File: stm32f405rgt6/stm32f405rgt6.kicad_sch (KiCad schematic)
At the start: 41 parts, among them J1 USART, J2 SWD, J3 I2C, J4 USB_OTG, J5 SPI, J6 AnalogInptus, J7 5V, J8 CAN, J9 3.3V, SW1 SW_Push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

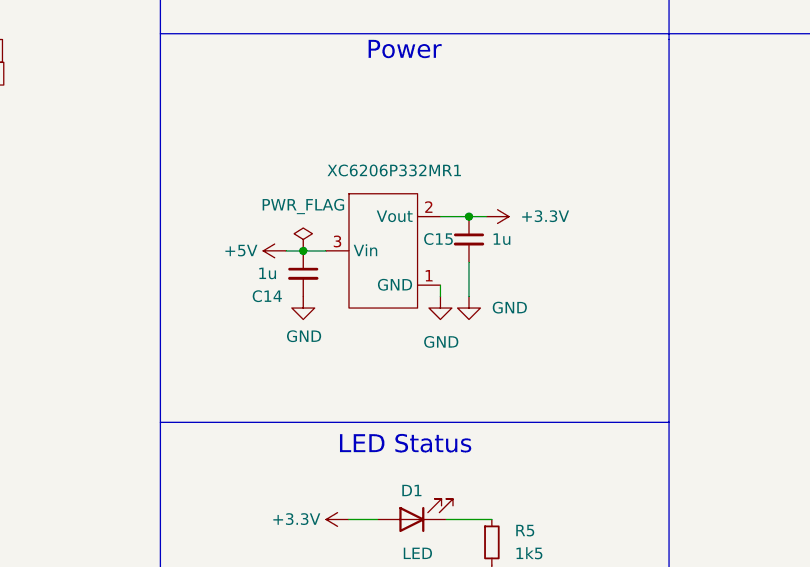
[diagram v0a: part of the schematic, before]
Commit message: reverted back to a version where the caps were not added to the voltage regulator
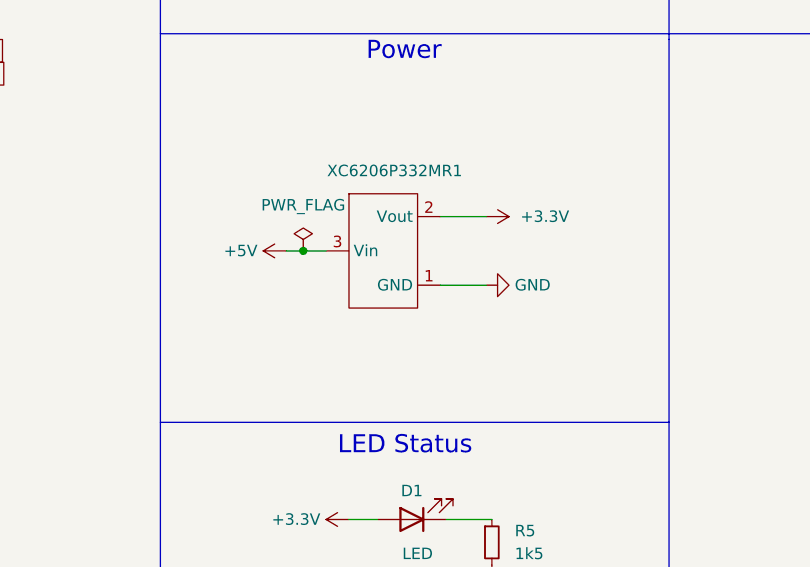
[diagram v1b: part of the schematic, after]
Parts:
- removed C14, C15: 1u, Capacitor_SMD:C_0603_1608Metric, symbol Device:C_Small
- J1: footprint Connector_PinHeader_2.54mm:PinHeader_1x04_P2.54mm_Vertical -> Connector_PinHeader_1.27mm:PinHeader_1x04_P1.27mm_Vertical
- J5: footprint TerminalBlock_Phoenix:TerminalBlock_Phoenix_MKDS-1,5-6_1x06_P5.00mm_Horizontal -> TerminalBlock_Phoenix:TerminalBlock_Phoenix_MKDS-1,5-6-5.08_1x06_P5.08mm_Horizontal
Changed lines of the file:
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@@
   (junction (at 20.955 72.39) (diameter 0) (color 0 0 0 0)
-  )
-  (junction (at 183.515 120.65) (diameter 0) (color 0 0 0 0)
   )
   (junction (at 41.91 167.64) (diameter 0) (color 0 0 0 0)
@@
     (stroke (width 0) (type default))
   )
+  (wire (pts (xy 180.34 128.27) (xy 185.42 128.27))
+    (stroke (width 0) (type default))
+  )
   (polyline (pts (xy 205.74 143.51) (xy 149.225 143.51))
     (stroke (width 0) (type default))
@@
     (stroke (width 0) (type default))
   )
-  (wire (pts (xy 183.515 129.54) (xy 183.515 125.73))
-    (stroke (width 0) (type default))
-  )
   (wire (pts (xy 22.86 146.685) (xy 45.085 146.685))
     (stroke (width 0) (type default))
@@
     (stroke (width 0) (type default))
   )
-  (wire (pts (xy 183.515 120.65) (xy 185.42 120.65))
-    (stroke (width 0) (type default))
-  )
   (wire (pts (xy 188.595 37.465) (xy 188.595 39.37))
     (stroke (width 0) (type default))
@@
     (stroke (width 0) (type default))
   )
-  (wire (pts (xy 180.34 129.54) (xy 180.34 128.27))
-    (stroke (width 0) (type default))
-  )
   (wire (pts (xy 99.06 90.17) (xy 101.6 90.17))
     (stroke (width 0) (type default))
@@
     (stroke (width 0) (type default))
   )
-  (wire (pts (xy 180.34 120.65) (xy 183.515 120.65))
+  (wire (pts (xy 180.34 120.65) (xy 185.42 120.65))
     (stroke (width 0) (type default))
   )
@@
     )
   )
-  (symbol (lib_id "power:GND") (at 165.1 129.54 0) (unit 1)
-    (in_bom yes) (on_board yes) (dnp no)
-    (property "Reference" "#PWR045" (at 165.1 135.89 0)
-      (effects (font (size 1.27 1.27)) hide)
-    )
-    (property "Value" "GND" (at 163.195 133.985 0)
-      (effects (font (size 1.27 1.27)) (justify left))
-    )
-    (property "Footprint" "" (at 165.1 129.54 0)
-      (effects (font (size 1.27 1.27)) hide)
-    )
-    (property "Datasheet" "" (at 165.1 129.54 0)
-      (effects (font (size 1.27 1.27)) hide)
-    )
-    (pin "1")
-    (instances
-      (project "stm32f405rgt6"
-        (path "/521c39b3-5842-46c1-bbd0-ab8aad1ee68c"
-          (reference "#PWR045") (unit 1)
-        )
-      )
-    )
-  )
   (symbol (lib_id "Custom:XC6206P332MR") (at 173.99 124.46 0) (unit 1)
     (in_bom yes) (on_board yes) (dnp no) (fields_autoplaced)
@@
       (effects (font (size 1.27 1.27)))
     )
-    (property "Footprint" "Connector_PinHeader_2.54mm:PinHeader_1x04_P2.54mm_Vertical" (at 24.765 37.465 0)
+    (property "Footprint" "Connector_PinHeader_1.27mm:PinHeader_1x04_P1.27mm_Vertical" (at 24.765 37.465 0)
       (effects (font (size 1.27 1.27)) hide)
     )
@@
     )
   )
-  (symbol (lib_id "power:GND") (at 180.34 129.54 0) (unit 1)
-    (in_bom yes) (on_board yes) (dnp no)
-    (property "Reference" "#PWR025" (at 180.34 135.89 0)
-      (effects (font (size 1.27 1.27)) hide)
-    )
-    (property "Value" "GND" (at 178.435 134.62 0)
-      (effects (font (size 1.27 1.27)) (justify left))
-    )
-    (property "Footprint" "" (at 180.34 129.54 0)
-      (effects (font (size 1.27 1.27)) hide)
-    )
-    (property "Datasheet" "" (at 180.34 129.54 0)
+  (symbol (lib_id "power:GND") (at 185.42 128.27 90) (unit 1)
+    (in_bom yes) (on_board yes) (dnp no) (fields_autoplaced)
+    (property "Reference" "#PWR025" (at 191.77 128.27 0)
+      (effects (font (size 1.27 1.27)) hide)
+    )
+    (property "Value" "GND" (at 188.595 128.27 90)
+      (effects (font (size 1.27 1.27)) (justify right))
+    )
+    (property "Footprint" "" (at 185.42 128.27 0)
+      (effects (font (size 1.27 1.27)) hide)
+    )
+    (property "Datasheet" "" (at 185.42 128.27 0)
       (effects (font (size 1.27 1.27)) hide)
     )
@@
         (path "/521c39b3-5842-46c1-bbd0-ab8aad1ee68c"
           (reference "C4") (unit 1)
-        )
-      )
-    )
-  )
-  (symbol (lib_id "Device:C_Small") (at 183.515 123.19 0) (unit 1)
-    (in_bom yes) (on_board yes) (dnp no)
-    (property "Reference" "C15" (at 178.435 123.19 0)
-      (effects (font (size 1.27 1.27)) (justify left))
-    )
-    (property "Value" "1u" (at 186.055 123.19 0)
-      (effects (font (size 1.27 1.27)) (justify left))
-    )
-    (property "Footprint" "Capacitor_SMD:C_0603_1608Metric" (at 183.515 123.19 0)
-      (effects (font (size 1.27 1.27)) hide)
-    )
-    (property "Datasheet" "~" (at 183.515 123.19 0)
-      (effects (font (size 1.27 1.27)) hide)
-    )
-    (pin "1")
-    (pin "2")
-    (instances
-      (project "stm32f405rgt6"
-        (path "/521c39b3-5842-46c1-bbd0-ab8aad1ee68c"
-          (reference "C15") (unit 1)
         )
       )
@@
     )
   )
-  (symbol (lib_id "Device:C_Small") (at 165.1 127 0) (unit 1)
-    (in_bom yes) (on_board yes) (dnp no)
-    (property "Reference" "C14" (at 159.385 129.54 0)
-      (effects (font (size 1.27 1.27)) (justify left))
-    )
-    (property "Value" "1u" (at 160.02 127 0)
-      (effects (font (size 1.27 1.27)) (justify left))
-    )
-    (property "Footprint" "Capacitor_SMD:C_0603_1608Metric" (at 165.1 127 0)
-      (effects (font (size 1.27 1.27)) hide)
-    )
-    (property "Datasheet" "~" (at 165.1 127 0)
-      (effects (font (size 1.27 1.27)) hide)
-    )
-    (pin "1")
-    (pin "2")
-    (instances
-      (project "stm32f405rgt6"
-        (path "/521c39b3-5842-46c1-bbd0-ab8aad1ee68c"
-          (reference "C14") (unit 1)
-        )
-      )
-    )
-  )
   (symbol (lib_id "Connector:USB_OTG") (at 95.885 40.64 0) (unit 1)
     (in_bom yes) (on_board yes) (dnp no) (fields_autoplaced)
@@
     )
   )
-  (symbol (lib_id "power:GND") (at 183.515 129.54 0) (unit 1)
-    (in_bom yes) (on_board yes) (dnp no) (fields_autoplaced)
-    (property "Reference" "#PWR041" (at 183.515 135.89 0)
-      (effects (font (size 1.27 1.27)) hide)
-    )
-    (property "Value" "GND" (at 186.055 130.81 0)
-      (effects (font (size 1.27 1.27)) (justify left))
-    )
-    (property "Footprint" "" (at 183.515 129.54 0)
-      (effects (font (size 1.27 1.27)) hide)
-    )
-    (property "Datasheet" "" (at 183.515 129.54 0)
-      (effects (font (size 1.27 1.27)) hide)
-    )
-    (pin "1")
-    (instances
-      (project "stm32f405rgt6"
-        (path "/521c39b3-5842-46c1-bbd0-ab8aad1ee68c"
-          (reference "#PWR041") (unit 1)
-        )
-      )
-    )
-  )
   (symbol (lib_id "power:GND") (at 76.2 171.45 0) (unit 1)
     (in_bom yes) (on_board yes) (dnp no) (fields_autoplaced)
@@
       (effects (font (size 1.27 1.27)))
     )
-    (property "Footprint" "TerminalBlock_Phoenix:TerminalBlock_Phoenix_MKDS-1,5-6_1x06_P5.00mm_Horizontal" (at 58.42 41.91 0)
-      (effects (font (size 1.27 1.27)) hide)
-    )
+    (property "Footprint" "TerminalBlock_Phoenix:TerminalBlock_Phoenix_MKDS-1,5-6-5.08_1x06_P5.08mm_Horizontal" (at 58.42 41.91 0)
+      (effects (font (size 1.27 1.27)) hide)
+    )

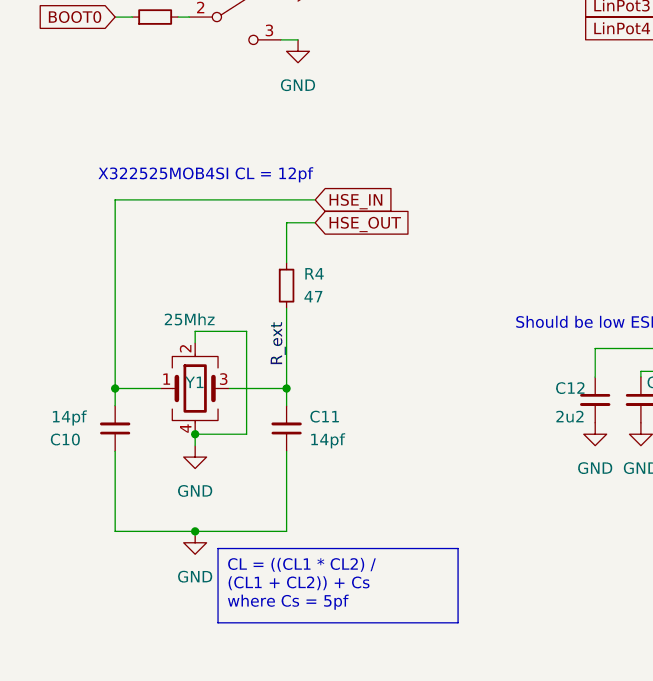
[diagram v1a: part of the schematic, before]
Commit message: added a new board for a more cost effective option
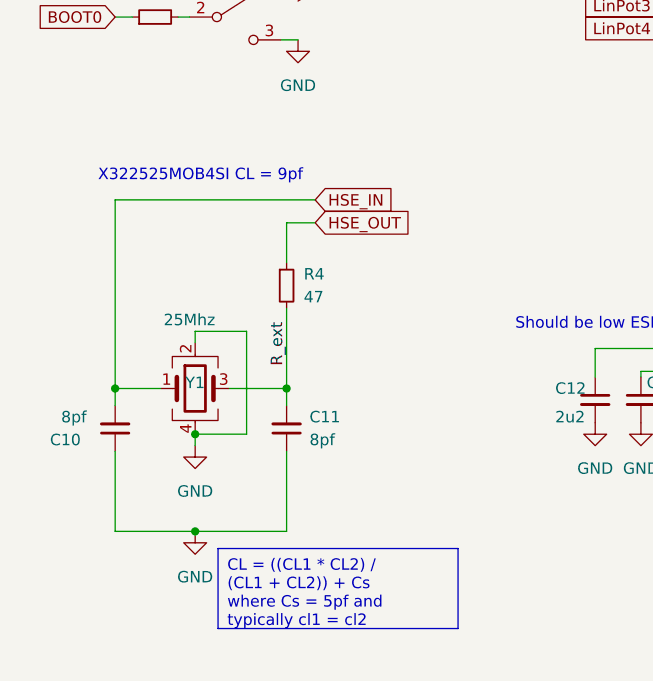
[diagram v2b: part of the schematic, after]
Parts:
- C10, C11: value 14pf -> 8pf
- SW1: footprint Button_Switch_SMD:SW_SPST_B3U-1000P-B -> Button_Switch_SMD:SW_SPST_PTS645
- SW2: footprint Button_Switch_SMD:SW_SPDT_PCM12 -> Button_Switch_SMD:SW_SPDT_CK-JS102011SAQN
- XC6206P332MR1: footprint Package_TO_SOT_SMD:SOT-23-3 -> Package_TO_SOT_SMD:SOT-223
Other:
- note added: "X322525MOB4SI CL = 9pf"
- note removed: "X322525MOB4SI CL = 12pf"
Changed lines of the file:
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@@
     (effects (font (size 0.85 0.85)) (justify left top))
   )
-  (text_box "CL = ((CL1 * CL2) / (CL1 + CL2)) + Cs  where Cs = 5pf"
-    (at 34.29 185.42 0) (size 26.67 8.255)
+  (text_box "CL = ((CL1 * CL2) / (CL1 + CL2)) + Cs  where Cs = 5pf and typically cl1 = cl2"
+    (at 34.29 185.42 0) (size 26.67 8.89)
     (stroke (width 0) (type default))
     (fill (type none))
@@
     (effects (font (size 1.27 1.27)) (justify left bottom))
   )
-  (text "X322525MOB4SI CL = 12pf\n" (at 20.955 144.78 0)
+  (text "X322525MOB4SI CL = 9pf\n" (at 20.955 144.78 0)
     (effects (font (size 1.27 1.27)) (justify left bottom))
   )
@@
       (effects (font (size 1.27 1.27)))
     )
-    (property "Footprint" "Package_TO_SOT_SMD:SOT-23-3" (at 173.99 124.46 0)
+    (property "Footprint" "Package_TO_SOT_SMD:SOT-223" (at 173.99 124.46 0)
       (effects (font (size 1.27 1.27)) hide)
     )
@@
       (effects (font (size 1.27 1.27)))
     )
-    (property "Footprint" "Button_Switch_SMD:SW_SPDT_PCM12" (at 36.195 126.365 0)
+    (property "Footprint" "Button_Switch_SMD:SW_SPDT_CK-JS102011SAQN" (at 36.195 126.365 0)
       (effects (font (size 1.27 1.27)) hide)
     )
@@
       (effects (font (size 1.27 1.27)) (justify right))
     )
-    (property "Value" "14pf" (at 44.45 173.3486 0)
+    (property "Value" "8pf" (at 44.45 173.3486 0)
       (effects (font (size 1.27 1.27)) (justify right))
     )
@@
       (effects (font (size 1.27 1.27)))
     )
-    (property "Footprint" "Button_Switch_SMD:SW_SPST_B3U-1000P-B" (at 28.575 95.25 0)
+    (property "Footprint" "Button_Switch_SMD:SW_SPST_PTS645" (at 28.575 95.25 0)
       (effects (font (size 1.27 1.27)) hide)
     )
@@
       (effects (font (size 1.27 1.27)) (justify left))
     )
-    (property "Value" "14pf" (at 19.685 170.815 0)
-      (effects (font (size 1.27 1.27)) (justify left))
-    )
+    (property "Value" "8pf" (at 19.685 170.815 0)
+      (effects (font (size 1.27 1.27)) (justify left))
+    )
